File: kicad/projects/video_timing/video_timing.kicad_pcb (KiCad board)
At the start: 2 copper layers, 203.2 x 97.8 mm, 26 parts, among them J1 peripheral_addr_bus_connector, J2 peripheral_aux_connector, J3 peripheral_membank_connector, U1 74HC161, U10 74HC30, U11 74HC30, U12 74HC30, U13 74HC30, U14 74HC30, U15 74HC30, U16 74HC30, U17 74HC30, U2 74HC161, U3 74HC161, U4 74HC161, U5 74HC161, U6 74HC04, U7 74HC04, U8 74HC00, U9 74HC00

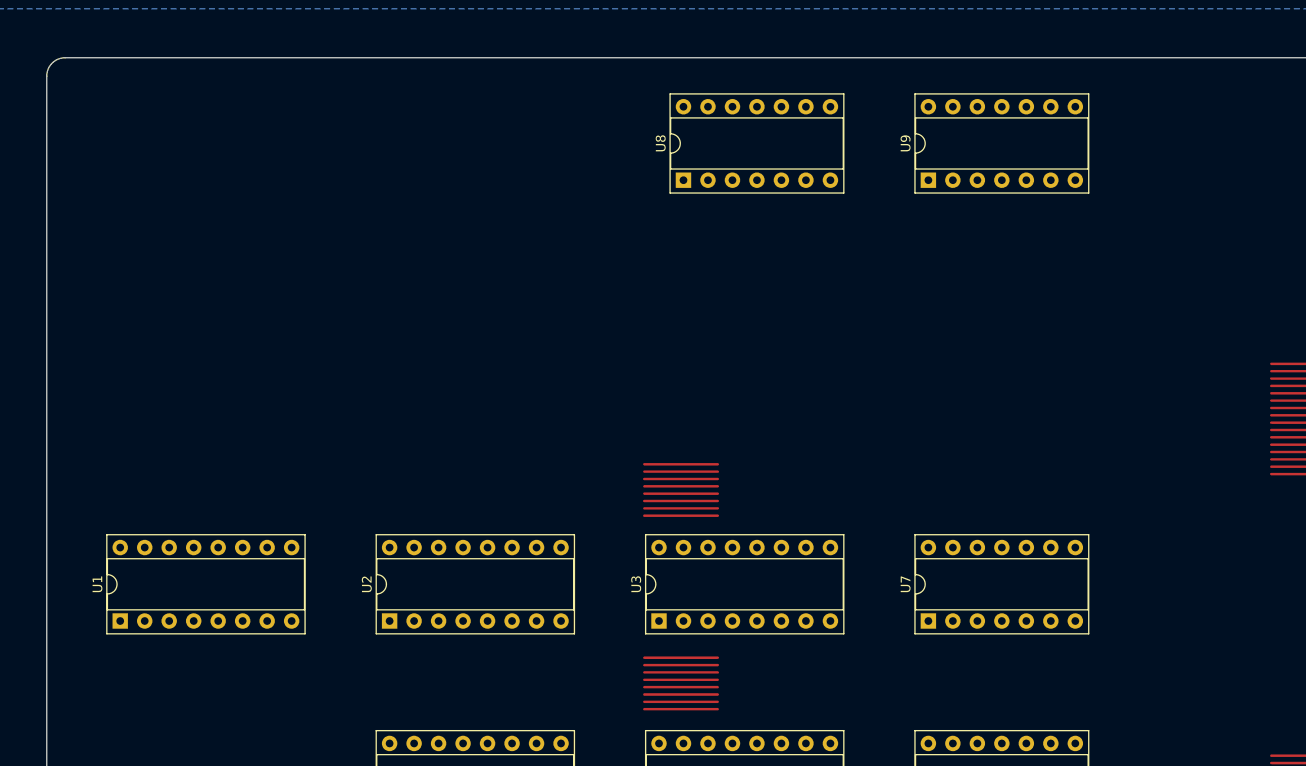
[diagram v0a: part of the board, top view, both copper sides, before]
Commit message: Roughing out the video baords - time to switch to 157s for bank sel as well.
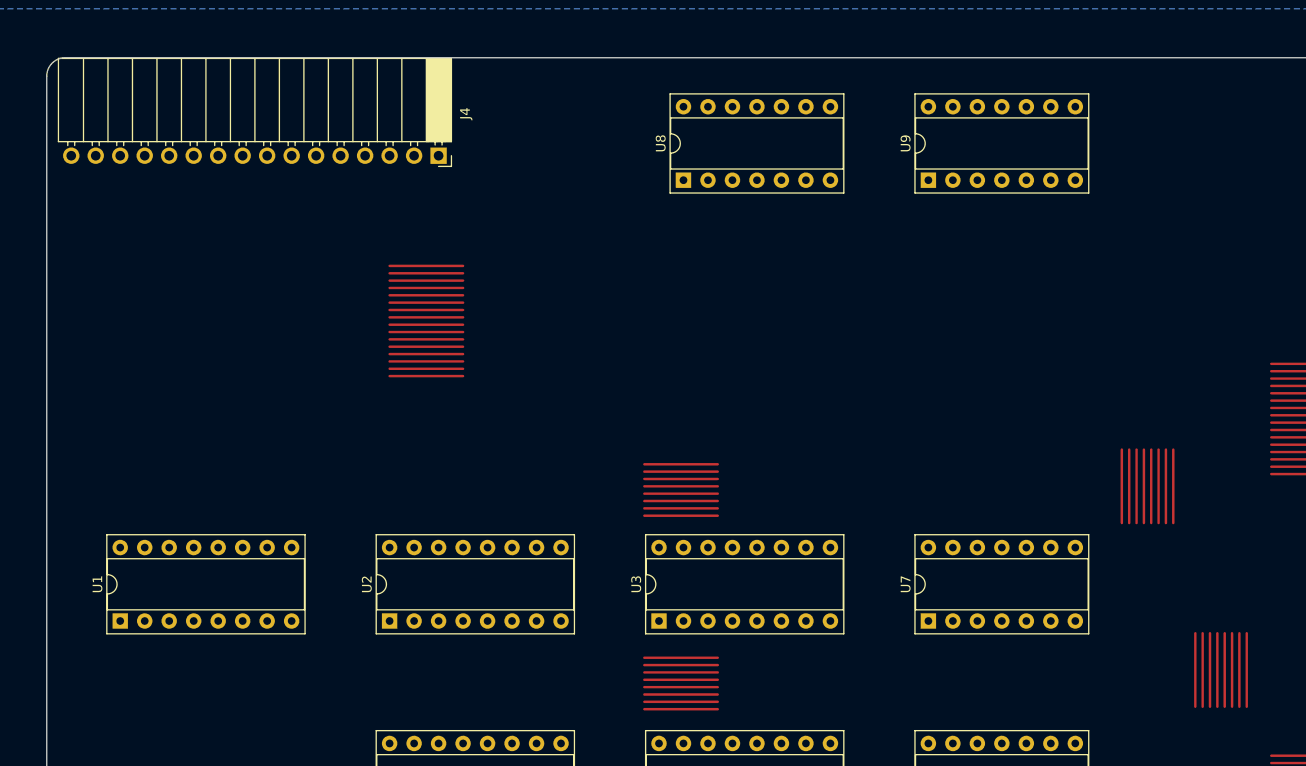
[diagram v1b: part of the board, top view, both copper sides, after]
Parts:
- added J4: Conn_01x16_Socket, Connector_PinSocket_2.54mm:PinSocket_1x16_P2.54mm_Horizontal, F.Cu at (91.4, 61.0)
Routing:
- net (no net): track 365.8 -> 609.6 mm

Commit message: Planning for video card.
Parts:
- added U18: 74HC161, Package_DIP:DIP-16_W7.62mm_Socket, F.Cu at (58.4, 114.3)
- added U19: 74HC27, Package_DIP:DIP-14_W7.62mm_Socket, F.Cu at (116.8, 94.0)
- added U20: 74HC27, Package_DIP:DIP-14_W7.62mm_Socket, F.Cu at (142.2, 94.0)
- added X1: CXO_DIP8, Oscillator:Oscillator_DIP-8, F.Cu at (59.7, 92.7)
- moved U1 25.4 mm to (58.4, 134.6)
- moved U10 12.7 mm to (195.6, 101.6)
- moved U14 12.7 mm to (195.6, 61.0)
- moved U11 10.2 mm to (210.8, 101.6)
- moved U15 10.2 mm to (210.8, 61.0)
- moved U12 7.62 mm to (226.1, 101.6)
- moved U16 7.62 mm to (226.1, 61.0)
- moved U13 5.08 mm to (241.3, 101.6)
- moved U17 5.08 mm to (241.3, 61.0)
- moved U4 5.08 mm to (86.4, 134.6)
- moved U5 5.08 mm to (114.3, 134.6)
- moved U6 5.08 mm to (142.2, 134.6)
- moved U2 5.08 mm to (86.4, 114.3)
- moved U3 5.08 mm to (114.3, 114.3)
- moved U7 5.08 mm to (142.2, 114.3)

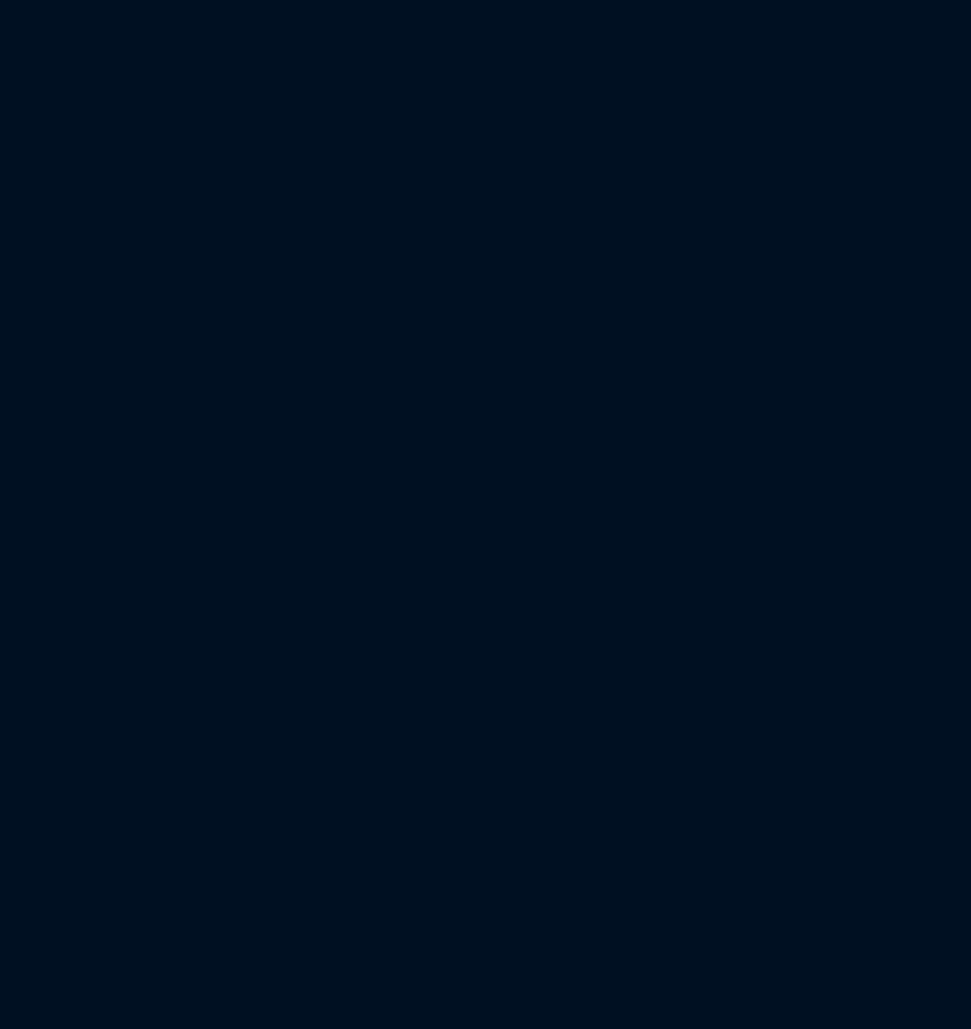
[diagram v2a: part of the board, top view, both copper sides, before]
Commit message: Schematic for video timing.
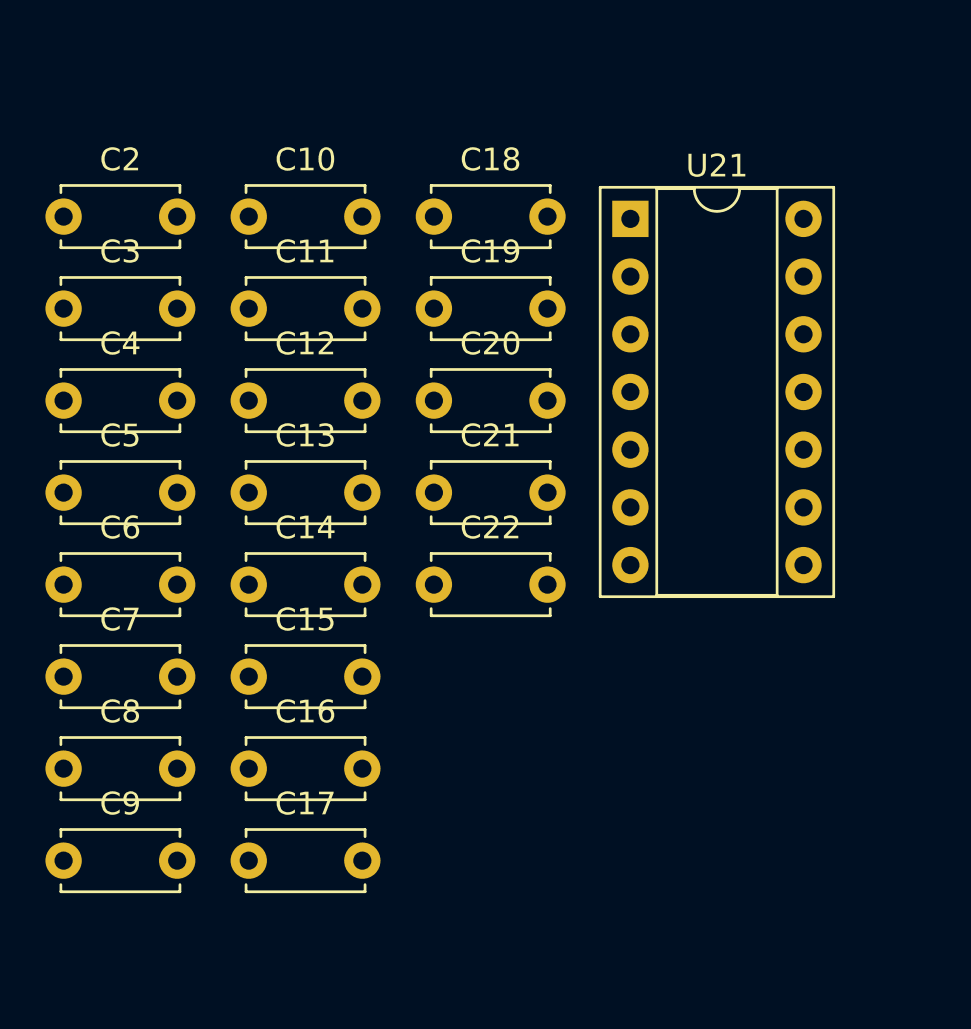
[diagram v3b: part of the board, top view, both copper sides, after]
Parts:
- added C10: C, Capacitor_THT:C_Disc_D5.0mm_W2.5mm_P5.00mm, F.Cu at (-42.2, 99.0)
- added C11: C, Capacitor_THT:C_Disc_D5.0mm_W2.5mm_P5.00mm, F.Cu at (-42.2, 103.0)
- added C12: C, Capacitor_THT:C_Disc_D5.0mm_W2.5mm_P5.00mm, F.Cu at (-42.2, 107.1)
- added C13: C, Capacitor_THT:C_Disc_D5.0mm_W2.5mm_P5.00mm, F.Cu at (-42.2, 111.1)
- added C14: C, Capacitor_THT:C_Disc_D5.0mm_W2.5mm_P5.00mm, F.Cu at (-42.2, 115.2)
- added C15: C, Capacitor_THT:C_Disc_D5.0mm_W2.5mm_P5.00mm, F.Cu at (-42.2, 119.2)
- added C16: C, Capacitor_THT:C_Disc_D5.0mm_W2.5mm_P5.00mm, F.Cu at (-42.2, 123.3)
- added C17: C, Capacitor_THT:C_Disc_D5.0mm_W2.5mm_P5.00mm, F.Cu at (-42.2, 127.3)
- added C18: C, Capacitor_THT:C_Disc_D5.0mm_W2.5mm_P5.00mm, F.Cu at (-34.0, 99.0)
- added C19: C, Capacitor_THT:C_Disc_D5.0mm_W2.5mm_P5.00mm, F.Cu at (-34.0, 103.0)
- added C2: C, Capacitor_THT:C_Disc_D5.0mm_W2.5mm_P5.00mm, F.Cu at (-50.4, 99.0)
- added C20: C, Capacitor_THT:C_Disc_D5.0mm_W2.5mm_P5.00mm, F.Cu at (-34.0, 107.1)
- added C21: C, Capacitor_THT:C_Disc_D5.0mm_W2.5mm_P5.00mm, F.Cu at (-34.0, 111.1)
- added C22: C, Capacitor_THT:C_Disc_D5.0mm_W2.5mm_P5.00mm, F.Cu at (-34.0, 115.2)
- added C3: C, Capacitor_THT:C_Disc_D5.0mm_W2.5mm_P5.00mm, F.Cu at (-50.4, 103.0)
- added C4: C, Capacitor_THT:C_Disc_D5.0mm_W2.5mm_P5.00mm, F.Cu at (-50.4, 107.1)
- added C5: C, Capacitor_THT:C_Disc_D5.0mm_W2.5mm_P5.00mm, F.Cu at (-50.4, 111.1)
- added C6: C, Capacitor_THT:C_Disc_D5.0mm_W2.5mm_P5.00mm, F.Cu at (-50.4, 115.2)
- added C7: C, Capacitor_THT:C_Disc_D5.0mm_W2.5mm_P5.00mm, F.Cu at (-50.4, 119.2)
- added C8: C, Capacitor_THT:C_Disc_D5.0mm_W2.5mm_P5.00mm, F.Cu at (-50.4, 123.3)
- added C9: C, Capacitor_THT:C_Disc_D5.0mm_W2.5mm_P5.00mm, F.Cu at (-50.4, 127.3)
- added U21: 74HC04, Package_DIP:DIP-14_W7.62mm_Socket, F.Cu at (-25.4, 99.1)
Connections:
- J1 pad 1: /DATA_BUS_00 -> unconnected-(J1-D_00-Pad1)
- J1 pad 10: /DATA_BUS_09 -> unconnected-(J1-D_09-Pad10)
- J1 pad 11: /DATA_BUS_10 -> unconnected-(J1-D_10-Pad11)
- J1 pad 12: /DATA_BUS_11 -> unconnected-(J1-D_11-Pad12)
- J1 pad 13: /DATA_BUS_12 -> unconnected-(J1-D_12-Pad13)
- J1 pad 14: /DATA_BUS_13 -> unconnected-(J1-D_13-Pad14)
- J1 pad 15: /DATA_BUS_14 -> unconnected-(J1-D_14-Pad15)
- J1 pad 16: /DATA_BUS_15 -> unconnected-(J1-D_15-Pad16)
- J1 pad 17: /ADDR_BUS_00 -> unconnected-(J1-A_00-Pad17)
- J1 pad 18: /ADDR_BUS_01 -> unconnected-(J1-A_01-Pad18)
- J1 pad 19: /ADDR_BUS_02 -> unconnected-(J1-A_02-Pad19)
- J1 pad 2: /DATA_BUS_01 -> unconnected-(J1-D_01-Pad2)
- J1 pad 20: /ADDR_BUS_03 -> unconnected-(J1-A_03-Pad20)
- J1 pad 21: /ADDR_BUS_04 -> unconnected-(J1-A_04-Pad21)
- J1 pad 22: /ADDR_BUS_05 -> unconnected-(J1-A_05-Pad22)
- J1 pad 23: /ADDR_BUS_06 -> unconnected-(J1-A_06-Pad23)
- J1 pad 24: /ADDR_BUS_07 -> unconnected-(J1-A_07-Pad24)
- J1 pad 25: /ADDR_BUS_08 -> unconnected-(J1-A_08-Pad25)
- J1 pad 26: /ADDR_BUS_09 -> unconnected-(J1-A_09-Pad26)
- J1 pad 27: /ADDR_BUS_10 -> unconnected-(J1-A_10-Pad27)
- J1 pad 28: /ADDR_BUS_11 -> unconnected-(J1-A_11-Pad28)
- J1 pad 29: /ADDR_BUS_12 -> unconnected-(J1-A_12-Pad29)
- J1 pad 3: /DATA_BUS_02 -> unconnected-(J1-D_02-Pad3)
- J1 pad 30: /ADDR_BUS_13 -> unconnected-(J1-A_13-Pad30)
- J1 pad 31: /ADDR_BUS_14 -> unconnected-(J1-A_14-Pad31)
- J1 pad 32: /ADDR_BUS_15 -> unconnected-(J1-A_15-Pad32)
- J1 pad 4: /DATA_BUS_03 -> unconnected-(J1-D_03-Pad4)
- J1 pad 5: /DATA_BUS_04 -> unconnected-(J1-D_04-Pad5)
- J1 pad 6: /DATA_BUS_05 -> unconnected-(J1-D_05-Pad6)
- J1 pad 7: /DATA_BUS_06 -> unconnected-(J1-D_06-Pad7)
- J1 pad 8: /DATA_BUS_07 -> unconnected-(J1-D_07-Pad8)
- J1 pad 9: /DATA_BUS_08 -> unconnected-(J1-D_08-Pad9)
- J3 pad 1: /BANK_BUS_00 -> unconnected-(J3-B_00-Pad1)
- J3 pad 10: /BANK_BUS_09 -> unconnected-(J3-B_09-Pad10)
- J3 pad 11: /BANK_BUS_10 -> unconnected-(J3-B_10-Pad11)
- J3 pad 12: /BANK_BUS_11 -> unconnected-(J3-B_11-Pad12)
- J3 pad 13: /BANK_BUS_12 -> unconnected-(J3-B_12-Pad13)
- J3 pad 14: /BANK_BUS_13 -> unconnected-(J3-B_13-Pad14)
- J3 pad 15: /BANK_BUS_14 -> unconnected-(J3-B_14-Pad15)
- J3 pad 16: /BANK_BUS_15 -> unconnected-(J3-B_15-Pad16)
- J3 pad 2: /BANK_BUS_01 -> unconnected-(J3-B_01-Pad2)
- J3 pad 3: /BANK_BUS_02 -> unconnected-(J3-B_02-Pad3)
- J3 pad 4: /BANK_BUS_03 -> unconnected-(J3-B_03-Pad4)
- J3 pad 5: /BANK_BUS_04 -> unconnected-(J3-B_04-Pad5)
- J3 pad 6: /BANK_BUS_05 -> unconnected-(J3-B_05-Pad6)
- J3 pad 7: /BANK_BUS_06 -> unconnected-(J3-B_06-Pad7)
- J3 pad 8: /BANK_BUS_07 -> unconnected-(J3-B_07-Pad8)
- J3 pad 9: /BANK_BUS_08 -> unconnected-(J3-B_08-Pad9)
- U1 pad 1: unconnected-(U1-~{MR}-Pad1) -> VCC
- U1 pad 10: unconnected-(U1-TE-Pad10) -> VCC
- U1 pad 13: unconnected-(U1-Q1-Pad13) -> Net-(U1-Q1)
- U1 pad 16: unconnected-(U1-VCC-Pad16) -> VCC
- U1 pad 2: unconnected-(U1-CP-Pad2) -> Net-(U1-CP)
- U1 pad 3: unconnected-(U1-P0-Pad3) -> GND
- U1 pad 4: unconnected-(U1-P1-Pad4) -> GND
- U1 pad 5: unconnected-(U1-P2-Pad5) -> GND
- U1 pad 6: unconnected-(U1-P3-Pad6) -> GND
- U1 pad 7: unconnected-(U1-PE-Pad7) -> VCC
- U1 pad 8: unconnected-(U1-GND-Pad8) -> GND
- U1 pad 9: unconnected-(U1-~{SPE}-Pad9) -> VCC
- U10 pad 1: unconnected-(U10A-A-Pad1) -> /~{COL_00}
- U10 pad 11: unconnected-(U10A-G-Pad11) -> /~{COL_06}
- U10 pad 12: unconnected-(U10A-H-Pad12) -> /~{COL_07}
- U10 pad 14: unconnected-(U10B-VCC-Pad14) -> VCC
- U10 pad 2: unconnected-(U10A-B-Pad2) -> /~{COL_01}
- U10 pad 3: unconnected-(U10A-C-Pad3) -> /~{COL_02}
- U10 pad 4: unconnected-(U10A-D-Pad4) -> /COL_03
- U10 pad 5: unconnected-(U10A-E-Pad5) -> /COL_04
- U10 pad 6: unconnected-(U10A-F-Pad6) -> /~{COL_05}
- U10 pad 7: unconnected-(U10B-GND-Pad7) -> GND
- U10 pad 8: unconnected-(U10A-~{Y}-Pad8) -> /~{COL_INDEX_24}
- U11 pad 1: unconnected-(U11A-A-Pad1) -> /~{COL_00}
- U11 pad 11: unconnected-(U11A-G-Pad11) -> /~{COL_06}
- U11 pad 12: unconnected-(U11A-H-Pad12) -> /~{COL_07}
- U11 pad 14: unconnected-(U11B-VCC-Pad14) -> VCC
- U11 pad 2: unconnected-(U11A-B-Pad2) -> /~{COL_01}
- U11 pad 3: unconnected-(U11A-C-Pad3) -> /COL_02
- U11 pad 4: unconnected-(U11A-D-Pad4) -> /~{COL_03}
- U11 pad 5: unconnected-(U11A-E-Pad5) -> /~{COL_04}
- U11 pad 6: unconnected-(U11A-F-Pad6) -> /COL_05
- U11 pad 7: unconnected-(U11B-GND-Pad7) -> GND
- U11 pad 8: unconnected-(U11A-~{Y}-Pad8) -> /~{COL_INDEX_36}
- U12 pad 1: unconnected-(U12A-A-Pad1) -> /~{COL_00}
- U12 pad 11: unconnected-(U12A-G-Pad11) -> /COL_06
- U12 pad 12: unconnected-(U12A-H-Pad12) -> /COL_07
- U12 pad 14: unconnected-(U12B-VCC-Pad14) -> VCC
- U12 pad 2: unconnected-(U12A-B-Pad2) -> /~{COL_01}
- U12 pad 3: unconnected-(U12A-C-Pad3) -> /COL_02
- U12 pad 4: unconnected-(U12A-D-Pad4) -> /~{COL_03}
- U12 pad 5: unconnected-(U12A-E-Pad5) -> /~{COL_04}
- U12 pad 6: unconnected-(U12A-F-Pad6) -> /~{COL_05}
- U12 pad 7: unconnected-(U12B-GND-Pad7) -> GND
- U12 pad 8: unconnected-(U12A-~{Y}-Pad8) -> /~{COL_INDEX_196}
- U13 pad 1: unconnected-(U13A-A-Pad1) -> /~{COL_00}
- U13 pad 11: unconnected-(U13A-G-Pad11) -> /COL_06
- U13 pad 12: unconnected-(U13A-H-Pad12) -> /COL_07
- U13 pad 14: unconnected-(U13B-VCC-Pad14) -> VCC
- U13 pad 2: unconnected-(U13A-B-Pad2) -> /~{COL_01}
- U13 pad 3: unconnected-(U13A-C-Pad3) -> /~{COL_02}
- U13 pad 4: unconnected-(U13A-D-Pad4) -> /COL_03
- U13 pad 5: unconnected-(U13A-E-Pad5) -> /~{COL_04}
- U13 pad 6: unconnected-(U13A-F-Pad6) -> /~{COL_05}
- U13 pad 7: unconnected-(U13B-GND-Pad7) -> GND
- U13 pad 8: unconnected-(U13A-~{Y}-Pad8) -> /~{COL_INDEX_200}
- U14 pad 1: unconnected-(U14A-A-Pad1) -> /~{ROW_00}
- U14 pad 11: unconnected-(U14A-G-Pad11) -> /~{ROW_09}
- U14 pad 12: unconnected-(U14A-H-Pad12) -> /~{ROW_04_06_07}
- U14 pad 14: unconnected-(U14B-VCC-Pad14) -> VCC
- U14 pad 2: unconnected-(U14A-B-Pad2) -> /ROW_01
- U14 pad 3: unconnected-(U14A-C-Pad3) -> /~{ROW_02}
- U14 pad 4: unconnected-(U14A-D-Pad4) -> /~{ROW_03}
- U14 pad 5: unconnected-(U14A-E-Pad5) -> /~{ROW_05}
- U14 pad 6: unconnected-(U14A-F-Pad6) -> /~{ROW_08}
- U14 pad 7: unconnected-(U14B-GND-Pad7) -> GND
- U14 pad 8: unconnected-(U14A-~{Y}-Pad8) -> /~{ROW_INDEX_2}
- U15 pad 1: unconnected-(U15A-A-Pad1) -> /ROW_00
- U15 pad 11: unconnected-(U15A-G-Pad11) -> /~{ROW_09}
- U15 pad 12: unconnected-(U15A-H-Pad12) -> /~{ROW_04_06_07}
- U15 pad 14: unconnected-(U15B-VCC-Pad14) -> VCC
- U15 pad 2: unconnected-(U15A-B-Pad2) -> /ROW_01
- U15 pad 3: unconnected-(U15A-C-Pad3) -> /~{ROW_02}
- U15 pad 4: unconnected-(U15A-D-Pad4) -> /~{ROW_03}
- U15 pad 5: unconnected-(U15A-E-Pad5) -> /ROW_05
- U15 pad 6: unconnected-(U15A-F-Pad6) -> /~{ROW_08}
- U15 pad 7: unconnected-(U15B-GND-Pad7) -> GND
- U15 pad 8: unconnected-(U15A-~{Y}-Pad8) -> /~{ROW_INDEX_35}
- U16 pad 1: unconnected-(U16A-A-Pad1) -> /ROW_00
- U16 pad 11: unconnected-(U16A-G-Pad11) -> /ROW_09
- U16 pad 12: unconnected-(U16A-H-Pad12) -> /~{ROW_04_06_07}
- U16 pad 14: unconnected-(U16B-VCC-Pad14) -> VCC
- U16 pad 2: unconnected-(U16A-B-Pad2) -> /ROW_01
- U16 pad 3: unconnected-(U16A-C-Pad3) -> /~{ROW_02}
- U16 pad 4: unconnected-(U16A-D-Pad4) -> /~{ROW_03}
- U16 pad 5: unconnected-(U16A-E-Pad5) -> /~{ROW_05}
- U16 pad 6: unconnected-(U16A-F-Pad6) -> /~{ROW_08}
- U16 pad 7: unconnected-(U16B-GND-Pad7) -> GND
- U16 pad 8: unconnected-(U16A-~{Y}-Pad8) -> /~{ROW_INDEX_515}
- U17 pad 1: unconnected-(U17A-A-Pad1) -> /ROW_00
- U17 pad 11: unconnected-(U17A-G-Pad11) -> /ROW_09
- U17 pad 12: unconnected-(U17A-H-Pad12) -> /~{ROW_04_06_07}
- U17 pad 14: unconnected-(U17B-VCC-Pad14) -> VCC
- U17 pad 2: unconnected-(U17A-B-Pad2) -> /~{ROW_01}
- U17 pad 3: unconnected-(U17A-C-Pad3) -> /ROW_02
- U17 pad 4: unconnected-(U17A-D-Pad4) -> /ROW_03
- U17 pad 5: unconnected-(U17A-E-Pad5) -> /~{ROW_05}
- U17 pad 6: unconnected-(U17A-F-Pad6) -> /~{ROW_08}
- U17 pad 7: unconnected-(U17B-GND-Pad7) -> GND
- U17 pad 8: unconnected-(U17A-~{Y}-Pad8) -> /~{ROW_INDEX_525}
- U18 pad 1: unconnected-(U18-~{MR}-Pad1) -> VCC
- U18 pad 10: unconnected-(U18-TE-Pad10) -> VCC
- U18 pad 13: unconnected-(U18-Q1-Pad13) -> /ROW_09
- U18 pad 14: unconnected-(U18-Q0-Pad14) -> /ROW_08
- U18 pad 16: unconnected-(U18-VCC-Pad16) -> VCC
- U18 pad 2: unconnected-(U18-CP-Pad2) -> /~{H_SYNC}
- U18 pad 3: unconnected-(U18-P0-Pad3) -> GND
- U18 pad 4: unconnected-(U18-P1-Pad4) -> GND
- U18 pad 5: unconnected-(U18-P2-Pad5) -> GND
- U18 pad 6: unconnected-(U18-P3-Pad6) -> GND
- U18 pad 7: unconnected-(U18-PE-Pad7) -> Net-(U18-PE)
- U18 pad 8: unconnected-(U18-GND-Pad8) -> GND
- U18 pad 9: unconnected-(U18-~{SPE}-Pad9) -> VCC
- U19 pad 1: unconnected-(U19-Pad1) -> /ROW_04
- U19 pad 10: unconnected-(U19-Pad10) -> GND
- U19 pad 11: unconnected-(U19-Pad11) -> GND
- U19 pad 12: unconnected-(U19-Pad12) -> /~{ROW_04_06_07}
- U19 pad 13: unconnected-(U19-Pad13) -> /ROW_07
- U19 pad 14: unconnected-(U19D-VCC-Pad14) -> VCC
- U19 pad 2: unconnected-(U19-Pad2) -> /ROW_06
- U19 pad 3: unconnected-(U19-Pad3) -> /H_BLANK
- U19 pad 4: unconnected-(U19-Pad4) -> /V_BLANK
- U19 pad 5: unconnected-(U19-Pad5) -> GND
- U19 pad 6: unconnected-(U19-Pad6) -> /~{ANY_BLANK}
- U19 pad 7: unconnected-(U19D-GND-Pad7) -> GND
- U19 pad 9: unconnected-(U19-Pad9) -> GND
- U2 pad 1: unconnected-(U2-~{MR}-Pad1) -> VCC
- U2 pad 10: unconnected-(U2-TE-Pad10) -> VCC
- U2 pad 11: unconnected-(U2-Q3-Pad11) -> /COL_03
- U2 pad 12: unconnected-(U2-Q2-Pad12) -> /COL_02
- U2 pad 13: unconnected-(U2-Q1-Pad13) -> /COL_01
- U2 pad 14: unconnected-(U2-Q0-Pad14) -> /COL_00
- U2 pad 15: unconnected-(U2-TC-Pad15) -> Net-(U2-TC)
- U2 pad 16: unconnected-(U2-VCC-Pad16) -> VCC
- U2 pad 2: unconnected-(U2-CP-Pad2) -> Net-(U1-Q1)
- U2 pad 3: unconnected-(U2-P0-Pad3) -> GND
- U2 pad 4: unconnected-(U2-P1-Pad4) -> GND
- U2 pad 5: unconnected-(U2-P2-Pad5) -> GND
- U2 pad 6: unconnected-(U2-P3-Pad6) -> GND
- U2 pad 7: unconnected-(U2-PE-Pad7) -> VCC
- U2 pad 8: unconnected-(U2-GND-Pad8) -> GND
- U2 pad 9: unconnected-(U2-~{SPE}-Pad9) -> VCC
- U3 pad 1: unconnected-(U3-~{MR}-Pad1) -> VCC
- U3 pad 10: unconnected-(U3-TE-Pad10) -> VCC
- U3 pad 11: unconnected-(U3-Q3-Pad11) -> /COL_07
- U3 pad 12: unconnected-(U3-Q2-Pad12) -> /COL_06
- U3 pad 13: unconnected-(U3-Q1-Pad13) -> /COL_05
- U3 pad 14: unconnected-(U3-Q0-Pad14) -> /COL_04
- U3 pad 16: unconnected-(U3-VCC-Pad16) -> VCC
- U3 pad 2: unconnected-(U3-CP-Pad2) -> Net-(U1-Q1)
- U3 pad 3: unconnected-(U3-P0-Pad3) -> GND
- U3 pad 4: unconnected-(U3-P1-Pad4) -> GND
- U3 pad 5: unconnected-(U3-P2-Pad5) -> GND
- U3 pad 6: unconnected-(U3-P3-Pad6) -> GND
- U3 pad 7: unconnected-(U3-PE-Pad7) -> Net-(U2-TC)
- U3 pad 8: unconnected-(U3-GND-Pad8) -> GND
- U3 pad 9: unconnected-(U3-~{SPE}-Pad9) -> VCC
- U4 pad 1: unconnected-(U4-~{MR}-Pad1) -> VCC
- U4 pad 10: unconnected-(U4-TE-Pad10) -> VCC
- U4 pad 11: unconnected-(U4-Q3-Pad11) -> /ROW_03
- U4 pad 12: unconnected-(U4-Q2-Pad12) -> /ROW_02
- U4 pad 13: unconnected-(U4-Q1-Pad13) -> /ROW_01
- U4 pad 14: unconnected-(U4-Q0-Pad14) -> /ROW_00
- U4 pad 15: unconnected-(U4-TC-Pad15) -> Net-(U4-TC)
- U4 pad 16: unconnected-(U4-VCC-Pad16) -> VCC
- U4 pad 2: unconnected-(U4-CP-Pad2) -> /~{H_SYNC}
- U4 pad 3: unconnected-(U4-P0-Pad3) -> GND
- U4 pad 4: unconnected-(U4-P1-Pad4) -> GND
- U4 pad 5: unconnected-(U4-P2-Pad5) -> GND
- U4 pad 6: unconnected-(U4-P3-Pad6) -> GND
- U4 pad 7: unconnected-(U4-PE-Pad7) -> VCC
- U4 pad 8: unconnected-(U4-GND-Pad8) -> GND
- U4 pad 9: unconnected-(U4-~{SPE}-Pad9) -> VCC
- U5 pad 1: unconnected-(U5-~{MR}-Pad1) -> VCC
- U5 pad 10: unconnected-(U5-TE-Pad10) -> VCC
- U5 pad 11: unconnected-(U5-Q3-Pad11) -> /ROW_07
- U5 pad 12: unconnected-(U5-Q2-Pad12) -> /ROW_06
- U5 pad 13: unconnected-(U5-Q1-Pad13) -> /ROW_05
- U5 pad 14: unconnected-(U5-Q0-Pad14) -> /ROW_04
- U5 pad 15: unconnected-(U5-TC-Pad15) -> Net-(U18-PE)
- U5 pad 16: unconnected-(U5-VCC-Pad16) -> VCC
- U5 pad 2: unconnected-(U5-CP-Pad2) -> /~{H_SYNC}
- U5 pad 3: unconnected-(U5-P0-Pad3) -> GND
- U5 pad 4: unconnected-(U5-P1-Pad4) -> GND
- U5 pad 5: unconnected-(U5-P2-Pad5) -> GND
- U5 pad 6: unconnected-(U5-P3-Pad6) -> GND
- U5 pad 7: unconnected-(U5-PE-Pad7) -> Net-(U4-TC)
- U5 pad 8: unconnected-(U5-GND-Pad8) -> GND
- U5 pad 9: unconnected-(U5-~{SPE}-Pad9) -> VCC
- U6 pad 1: unconnected-(U6-Pad1) -> /COL_00
- U6 pad 10: unconnected-(U6-Pad10) -> /~{COL_04}
- U6 pad 11: unconnected-(U6-Pad11) -> /COL_04
- U6 pad 12: unconnected-(U6-Pad12) -> /~{COL_05}
- U6 pad 13: unconnected-(U6-Pad13) -> /COL_05
- U6 pad 14: unconnected-(U6G-VCC-Pad14) -> VCC
- U6 pad 2: unconnected-(U6-Pad2) -> /~{COL_00}
- U6 pad 3: unconnected-(U6-Pad3) -> /COL_01
- U6 pad 4: unconnected-(U6-Pad4) -> /~{COL_01}
- U6 pad 5: unconnected-(U6-Pad5) -> /COL_02
- U6 pad 6: unconnected-(U6-Pad6) -> /~{COL_02}
- U6 pad 7: unconnected-(U6G-GND-Pad7) -> GND
- U6 pad 8: unconnected-(U6-Pad8) -> /~{COL_03}
- U6 pad 9: unconnected-(U6-Pad9) -> /COL_03
- U7 pad 1: unconnected-(U7-Pad1) -> /COL_06
- U7 pad 10: unconnected-(U7-Pad10) -> /~{ROW_02}
- U7 pad 11: unconnected-(U7-Pad11) -> /ROW_02
- U7 pad 12: unconnected-(U7-Pad12) -> /~{ROW_03}
- U7 pad 13: unconnected-(U7-Pad13) -> /ROW_03
- U7 pad 14: unconnected-(U7G-VCC-Pad14) -> VCC
- U7 pad 2: unconnected-(U7-Pad2) -> /~{COL_06}
- U7 pad 3: unconnected-(U7-Pad3) -> /COL_07
- U7 pad 4: unconnected-(U7-Pad4) -> /~{COL_07}
- U7 pad 5: unconnected-(U7-Pad5) -> /ROW_00
- U7 pad 6: unconnected-(U7-Pad6) -> /~{ROW_00}
- U7 pad 7: unconnected-(U7G-GND-Pad7) -> GND
- U7 pad 8: unconnected-(U7-Pad8) -> /~{ROW_01}
- U7 pad 9: unconnected-(U7-Pad9) -> /ROW_01
- U8 pad 1: unconnected-(U8-Pad1) -> /~{COL_INDEX_24}
- U8 pad 10: unconnected-(U8-Pad10) -> Net-(U8-Pad10)
- U8 pad 11: unconnected-(U8-Pad11) -> Net-(U8-Pad10)
- U8 pad 12: unconnected-(U8-Pad12) -> /H_BLANK
- U8 pad 13: unconnected-(U8-Pad13) -> /~{COL_INDEX_36}
- U8 pad 14: unconnected-(U8E-VCC-Pad14) -> VCC
- U8 pad 2: unconnected-(U8-Pad2) -> /~{H_SYNC}
- U8 pad 3: unconnected-(U8-Pad3) -> /H_SYNC
- U8 pad 4: unconnected-(U8-Pad4) -> /H_SYNC
- U8 pad 5: unconnected-(U8-Pad5) -> /~{COL_INDEX_200}
- U8 pad 6: unconnected-(U8-Pad6) -> /~{H_SYNC}
- U8 pad 7: unconnected-(U8E-GND-Pad7) -> GND
- U8 pad 8: unconnected-(U8-Pad8) -> /H_BLANK
- U8 pad 9: unconnected-(U8-Pad9) -> /~{COL_INDEX_196}
- U9 pad 1: unconnected-(U9-Pad1) -> /~{ROW_INDEX_2}
- U9 pad 10: unconnected-(U9-Pad10) -> Net-(U9-Pad10)
- U9 pad 11: unconnected-(U9-Pad11) -> Net-(U9-Pad10)
- U9 pad 12: unconnected-(U9-Pad12) -> /V_BLANK
- U9 pad 13: unconnected-(U9-Pad13) -> /~{ROW_INDEX_35}
- U9 pad 14: unconnected-(U9E-VCC-Pad14) -> VCC
- U9 pad 2: unconnected-(U9-Pad2) -> Net-(U9-Pad2)
- U9 pad 3: unconnected-(U9-Pad3) -> /V_SYNC
- U9 pad 4: unconnected-(U9-Pad4) -> /V_SYNC
- U9 pad 5: unconnected-(U9-Pad5) -> /~{ROW_INDEX_525}
- U9 pad 6: unconnected-(U9-Pad6) -> Net-(U9-Pad2)
- U9 pad 7: unconnected-(U9E-GND-Pad7) -> GND
- U9 pad 8: unconnected-(U9-Pad8) -> /V_BLANK
- U9 pad 9: unconnected-(U9-Pad9) -> /~{ROW_INDEX_515}
- X1 pad 4: unconnected-(X1-GND-Pad4) -> GND
- X1 pad 5: unconnected-(X1-OUT-Pad5) -> Net-(U1-CP)
- X1 pad 8: unconnected-(X1-Vcc-Pad8) -> VCC

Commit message: Start laying out video timing.
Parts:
- removed U19: 74HC27, Package_DIP:DIP-14_W7.62mm_Socket
- U20: value 74HC27 -> 74HC11
- moved U21 168.3 mm to (142.2, 114.3), turned to 90 degrees
- moved U18 55.9 mm to (114.3, 114.3)
- moved U5 49.3 mm to (86.4, 94.0)
- moved U20 25.4 mm to (116.8, 94.0)
- moved X1 21.6 mm to (58.4, 114.3)
- moved U2 20.3 mm to (86.4, 134.6)
- moved U3 20.3 mm to (114.3, 134.6)
- moved U4 20.3 mm to (86.4, 114.3)
- moved U7 20.3 mm to (142.2, 94.0)
- moved U10 5.08 mm to (195.6, 106.7)
- moved U11 5.08 mm to (210.8, 106.7)
- moved U12 5.08 mm to (226.1, 106.7)
- moved U13 5.08 mm to (241.3, 106.7)
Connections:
- J4 pad 1: unconnected-(J4-Pin_1-Pad1) -> /ROW_02
- J4 pad 10: unconnected-(J4-Pin_10-Pad10) -> /COL_01
- J4 pad 11: unconnected-(J4-Pin_11-Pad11) -> /COL_02
- J4 pad 12: unconnected-(J4-Pin_12-Pad12) -> /COL_03
- J4 pad 13: unconnected-(J4-Pin_13-Pad13) -> /COL_04
- J4 pad 14: unconnected-(J4-Pin_14-Pad14) -> /COL_05
- J4 pad 15: unconnected-(J4-Pin_15-Pad15) -> /COL_06
- J4 pad 16: unconnected-(J4-Pin_16-Pad16) -> /COL_07
- J4 pad 2: unconnected-(J4-Pin_2-Pad2) -> /ROW_03
- J4 pad 3: unconnected-(J4-Pin_3-Pad3) -> /ROW_04
- J4 pad 4: unconnected-(J4-Pin_4-Pad4) -> /ROW_05
- J4 pad 5: unconnected-(J4-Pin_5-Pad5) -> /ROW_06
- J4 pad 6: unconnected-(J4-Pin_6-Pad6) -> /ROW_07
- J4 pad 7: unconnected-(J4-Pin_7-Pad7) -> /ROW_08
- J4 pad 8: unconnected-(J4-Pin_8-Pad8) -> /ROW_09
- J4 pad 9: unconnected-(J4-Pin_9-Pad9) -> /COL_00
- U1 pad 13: Net-(U1-Q1) -> /PIXEL_CLOCK
- U10 pad 12: /~{COL_07} -> /COL_07
- U10 pad 4: /COL_03 -> /~{COL_03}
- U10 pad 5: /COL_04 -> /~{COL_04}
- U10 pad 6: /~{COL_05} -> /COL_05
- U10 pad 8: /~{COL_INDEX_24} -> /~{COL_INDEX_160}
- U11 pad 12: /~{COL_07} -> /COL_07
- U11 pad 8: /~{COL_INDEX_36} -> /~{COL_INDEX_164}
- U12 pad 11: /COL_06 -> /~{COL_06}
- U12 pad 4: /~{COL_03} -> /COL_03
- U12 pad 5: /~{COL_04} -> /COL_04
- U12 pad 6: /~{COL_05} -> /COL_05
- U12 pad 8: /~{COL_INDEX_196} -> /~{COL_INDEX_188}
- U14 pad 12: /~{ROW_04_06_07} -> /ROW_05_06_07
- U14 pad 2: /ROW_01 -> /~{ROW_01}
- U14 pad 5: /~{ROW_05} -> /~{ROW_04}
- U14 pad 6: /~{ROW_08} -> /ROW_08
- U14 pad 8: /~{ROW_INDEX_2} -> /~{ROW_INDEX_480}
- U15 pad 1: /ROW_00 -> /~{ROW_00}
- U15 pad 12: /~{ROW_04_06_07} -> /ROW_05_06_07
- U15 pad 4: /~{ROW_03} -> /ROW_03
- U15 pad 5: /ROW_05 -> /~{ROW_04}
- U15 pad 6: /~{ROW_08} -> /ROW_08
- U15 pad 8: /~{ROW_INDEX_35} -> /~{ROW_INDEX_490}
- U16 pad 1: /ROW_00 -> /~{ROW_00}
- U16 pad 11: /ROW_09 -> /~{ROW_09}
- U16 pad 12: /~{ROW_04_06_07} -> /ROW_05_06_07
- U16 pad 2: /ROW_01 -> /~{ROW_01}
- U16 pad 3: /~{ROW_02} -> /ROW_02
- U16 pad 4: /~{ROW_03} -> /ROW_03
- U16 pad 5: /~{ROW_05} -> /~{ROW_04}
- U16 pad 6: /~{ROW_08} -> /ROW_08
- U16 pad 8: /~{ROW_INDEX_515} -> /~{ROW_INDEX_492}
- U17 pad 12: /~{ROW_04_06_07} -> VCC
- U17 pad 5: /~{ROW_05} -> /~{ROW_04}
- U18 pad 1: VCC -> /~{ROW_INDEX_525}
- U2 pad 1: VCC -> /~{COL_INDEX_200}
- U2 pad 2: Net-(U1-Q1) -> /PIXEL_CLOCK
- U20 pad 1: unconnected-(U20-Pad1) -> GND
- U20 pad 10: unconnected-(U20-Pad10) -> GND
- U20 pad 11: unconnected-(U20-Pad11) -> GND
- U20 pad 13: unconnected-(U20-Pad13) -> GND
- U20 pad 14: unconnected-(U20D-VCC-Pad14) -> VCC
- U20 pad 2: unconnected-(U20-Pad2) -> GND
- U20 pad 3: unconnected-(U20-Pad3) -> /ROW_05
- U20 pad 4: unconnected-(U20-Pad4) -> /ROW_06
- U20 pad 5: unconnected-(U20-Pad5) -> /ROW_07
- U20 pad 6: unconnected-(U20-Pad6) -> /ROW_05_06_07
- U20 pad 7: unconnected-(U20D-GND-Pad7) -> GND
- U20 pad 9: unconnected-(U20-Pad9) -> GND
- U21 pad 1: /ROW_05 -> /COL_06
- U21 pad 12: /ANY_BLANK -> /~{ROW_09}
- U21 pad 13: /~{ANY_BLANK} -> /ROW_09
- U21 pad 2: /~{ROW_05} -> /~{COL_06}
- U21 pad 3: /ROW_08 -> /COL_00
- U21 pad 4: /~{ROW_08} -> /~{COL_00}
- U21 pad 5: /ROW_09 -> GND
- U21 pad 6: /~{ROW_09} -> unconnected-(U21-Pad6)
- U3 pad 1: VCC -> /~{COL_INDEX_200}
- U3 pad 2: Net-(U1-Q1) -> /PIXEL_CLOCK
- U4 pad 1: VCC -> /~{ROW_INDEX_525}
- U5 pad 1: VCC -> /~{ROW_INDEX_525}
- U6 pad 1: /COL_00 -> /PIXEL_CLOCK
- U6 pad 2: /~{COL_00} -> /~{PIXEL_CLOCK}
- U7 pad 1: /COL_06 -> /ROW_08
- U7 pad 10: /~{ROW_02} -> /~{ROW_03}
- U7 pad 11: /ROW_02 -> /ROW_03
- U7 pad 12: /~{ROW_03} -> /~{ROW_04}
- U7 pad 13: /ROW_03 -> /ROW_04
- U7 pad 2: /~{COL_06} -> /~{ROW_08}
- U7 pad 3: /COL_07 -> /ROW_00
- U7 pad 4: /~{COL_07} -> /~{ROW_00}
- U7 pad 5: /ROW_00 -> /ROW_01
- U7 pad 6: /~{ROW_00} -> /~{ROW_01}
- U7 pad 8: /~{ROW_01} -> /~{ROW_02}
- U7 pad 9: /ROW_01 -> /ROW_02
- U8 pad 1: /~{COL_INDEX_24} -> /~{COL_INDEX_188}
- U8 pad 13: /~{COL_INDEX_36} -> /~{COL_INDEX_200}
- U8 pad 5: /~{COL_INDEX_200} -> /~{COL_INDEX_164}
- U8 pad 9: /~{COL_INDEX_196} -> /~{COL_INDEX_160}
- U9 pad 1: /~{ROW_INDEX_2} -> /~{ROW_INDEX_492}
- U9 pad 13: /~{ROW_INDEX_35} -> /~{ROW_INDEX_525}
- U9 pad 5: /~{ROW_INDEX_525} -> /~{ROW_INDEX_490}
- U9 pad 9: /~{ROW_INDEX_515} -> /~{ROW_INDEX_480}
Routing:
- net (no net): track 609.6 -> 15.2 mm
- net /ROW_02: track 0.00 -> 101.6 mm
- net /ROW_03: track 0.00 -> 98.3 mm
- net /ROW_04: track 0.00 -> 97.5 mm
- net /ROW_05: track 0.00 -> 94.2 mm
- net /COL_02: track 0.00 -> 92.5 mm
- net /COL_00: track 0.00 -> 91.4 mm
- net /ROW_06: track 0.00 -> 90.9 mm
- net /COL_03: track 0.00 -> 89.2 mm
- net /COL_01: track 0.00 -> 88.1 mm
- net /ROW_07: track 0.00 -> 87.6 mm
- net /ROW_08: track 0.00 -> 74.2 mm
- net /ROW_09: track 0.00 -> 69.6 mm
- net /COL_04: track 0.00 -> 68.1 mm
- net /ROW_01: track 0.00 -> 66.0 mm
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
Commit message: Bit more tweaking and fleshing out of video circuits.
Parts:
- moved C17 292.7 mm to (250.2, 114.3), turned to -90 degrees
- moved C22 286.6 mm to (250.2, 78.7), turned to -90 degrees
- moved C16 280.7 mm to (234.9, 78.7), turned to -90 degrees
- moved C21 269.0 mm to (234.9, 114.3), turned to -90 degrees
- moved C15 265.0 mm to (219.7, 78.7), turned to -90 degrees
- moved C20 253.9 mm to (219.7, 114.3), turned to -90 degrees
- moved C14 249.3 mm to (204.5, 78.7), turned to -90 degrees
- moved C18 239.0 mm to (204.5, 114.3), turned to -90 degrees
- moved C4 188.2 mm to (137.2, 91.4), turned to 90 degrees
- moved C5 187.5 mm to (137.2, 111.7), turned to 90 degrees
- moved C9 187.5 mm to (137.2, 127.0), turned to -90 degrees
- moved C2 162.3 mm to (111.8, 91.4), turned to 90 degrees
- moved C6 159.6 mm to (109.2, 111.7), turned to 90 degrees
- moved J4 154.9 mm to (246.4, 61.0)
- moved C10 154.0 mm to (109.2, 127.0), turned to -90 degrees
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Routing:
- net /ROW_09: track 69.6 -> 77.2 mm
- net /ROW_08: track 74.2 -> 81.8 mm
- net /ROW_03: track 98.3 -> 105.9 mm
- net GND: track 0.00 -> 7.62 mm
- net /ROW_07: track 87.6 -> 95.2 mm
- net /ROW_06: track 90.9 -> 98.6 mm
- net /ROW_05: track 94.2 -> 101.9 mm
- net /ROW_04: track 97.5 -> 105.2 mm
- net /COL_07: track 58.2 -> 65.8 mm
- net /COL_06: track 61.5 -> 69.1 mm
- net /COL_05: track 64.8 -> 72.4 mm
- net /COL_04: track 68.1 -> 75.7 mm
- net /COL_03: track 89.2 -> 96.8 mm
- net /COL_02: track 92.5 -> 100.1 mm
- net /COL_01: track 88.1 -> 95.8 mm
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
